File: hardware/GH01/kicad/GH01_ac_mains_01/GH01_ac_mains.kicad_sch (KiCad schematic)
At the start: 10 parts, among them Q1 BS170, U1 XIAO ESP32C3

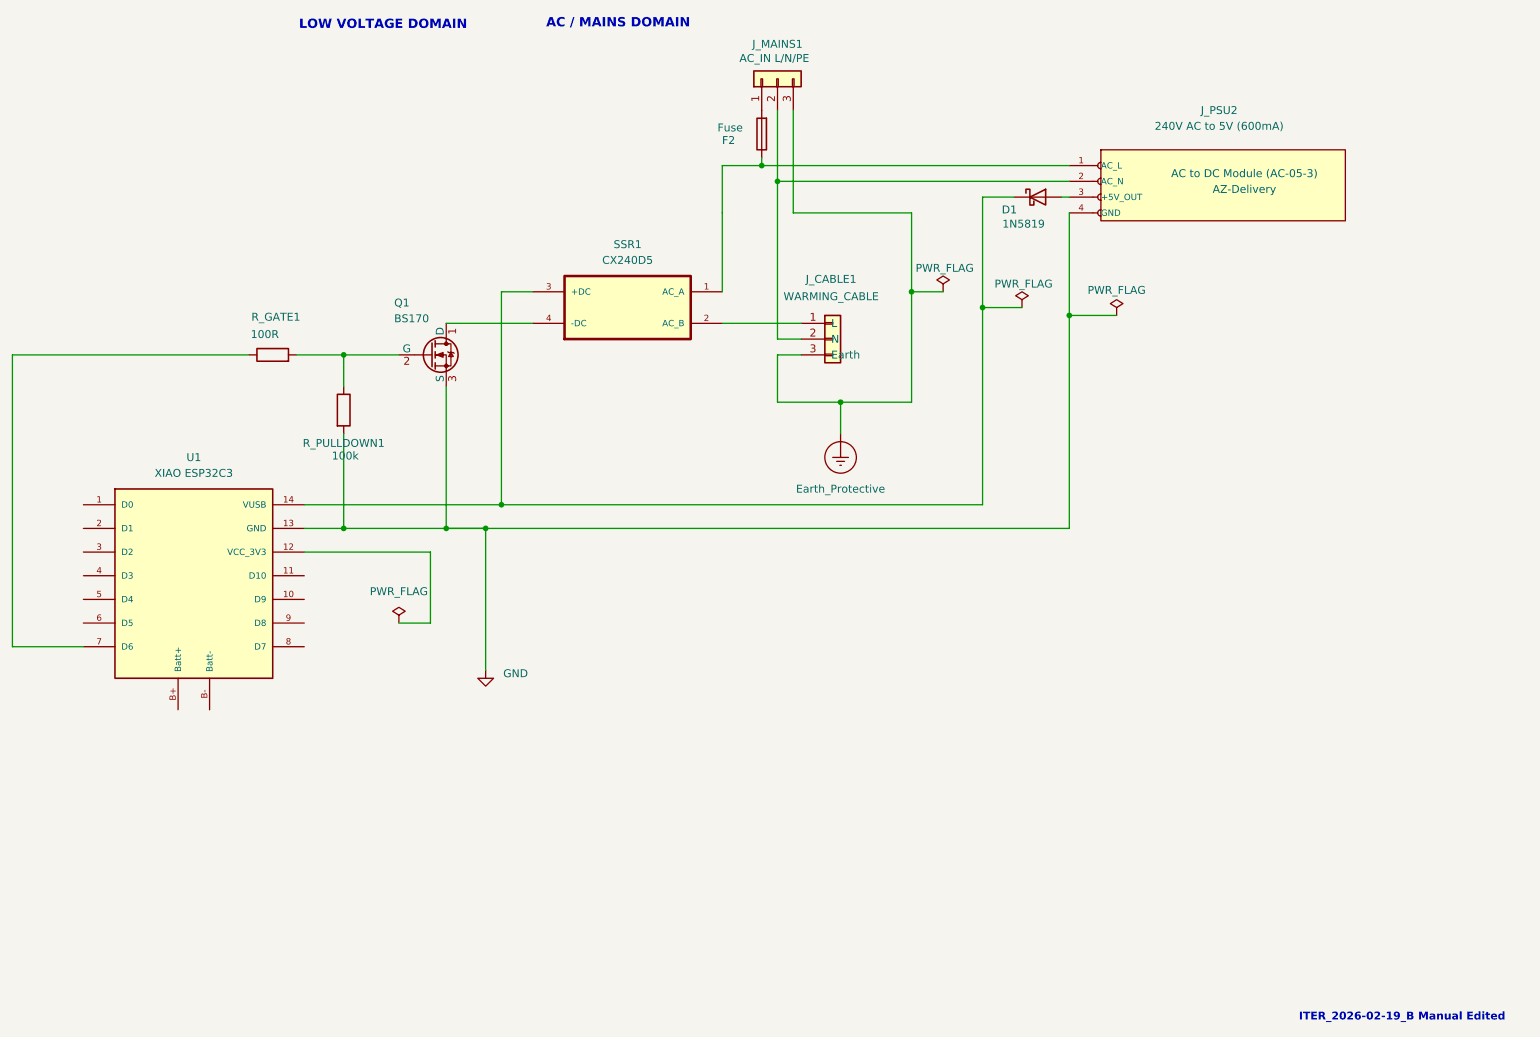
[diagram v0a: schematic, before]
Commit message: GH01 split AC/LV scaffold and interface validation
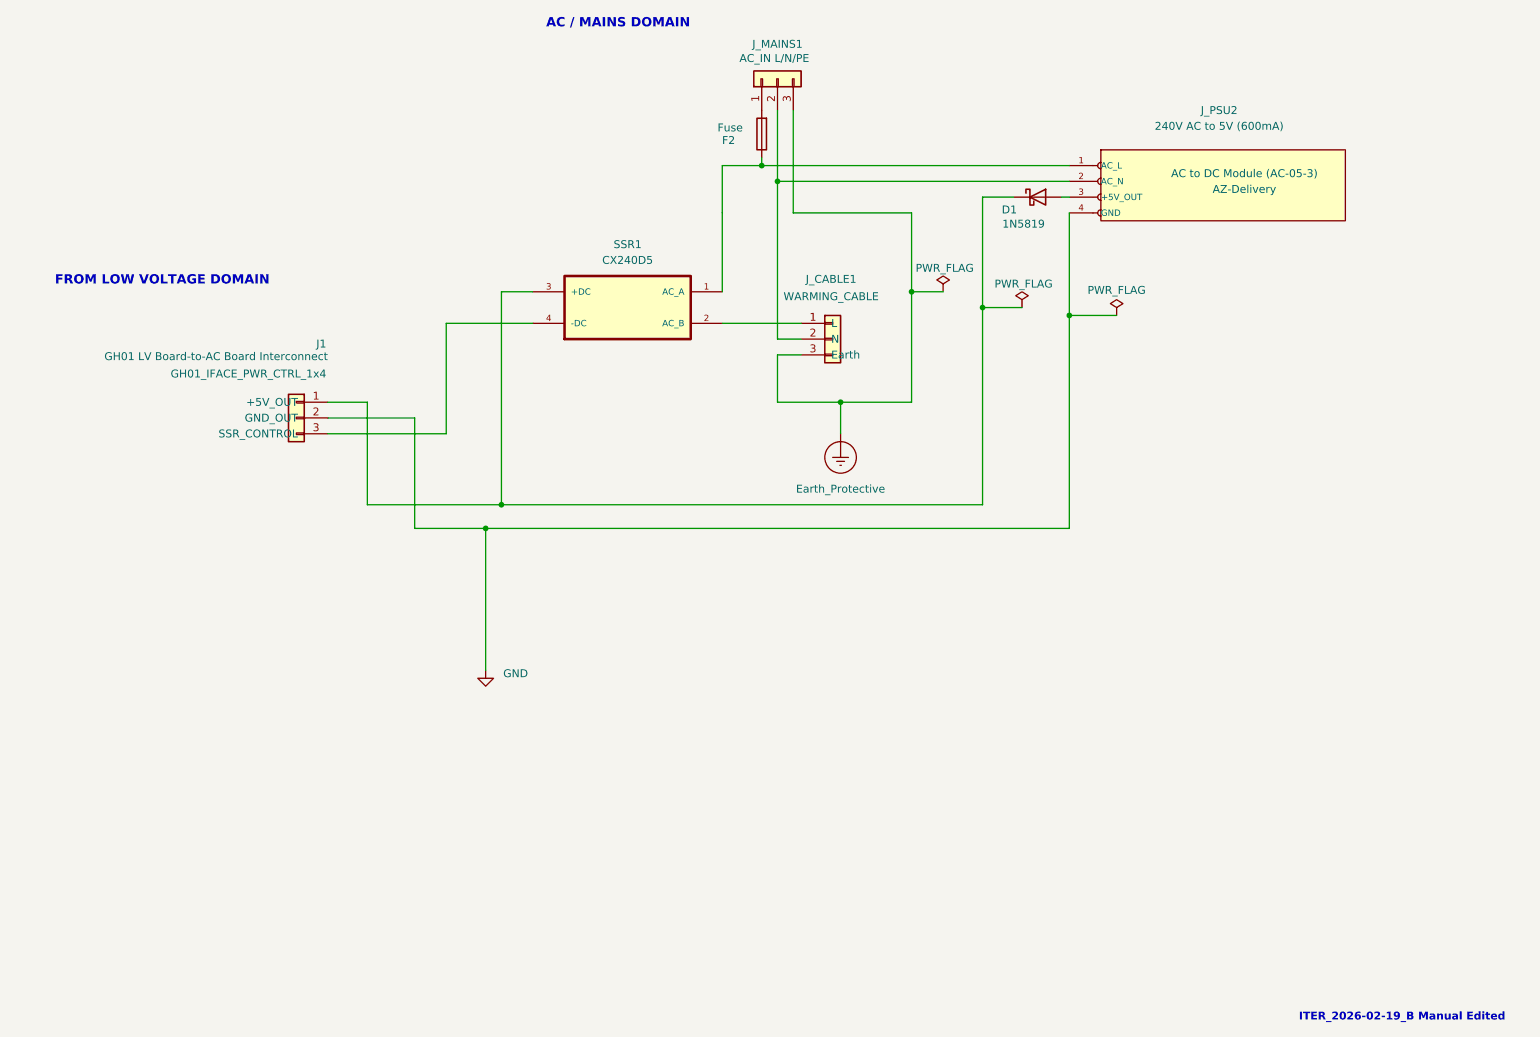
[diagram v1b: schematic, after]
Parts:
- removed Q1: BS170, Package_TO_SOT_THT:TO-92_Inline, symbol Transistor_FET:BS170
- removed R_GATE1: 100R, symbol Device:R
- removed R_PULLDOWN1: 100k, symbol Device:R
- removed U1: XIAO ESP32C3, XIAO_ESP32C3:ESP32-C3, symbol xiao_esp32c3:XIAO ESP32C3
- added J1: GH01_IFACE_PWR_CTRL_1x4, symbol GH01_custom:GH01_IFACE_PWR_CTRL_1x4
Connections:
- net GND: now also J1.2 (GND_OUT)
- net at D1.1 (K), SSR1.3 (+DC): now also J1.1 (+5V_OUT)
- net at SSR1.4 (-DC): now also J1.3 (SSR_CONTROL)
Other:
- note added: "FROM LOW VOLTAGE DOMAIN"
- note removed: "LOW VOLTAGE DOMAIN"
